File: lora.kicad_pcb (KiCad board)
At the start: 4 copper layers, 80.5 x 45 mm, 64 parts, among them J1 Conn_01x02, J11 Conn_Coaxial, J2 Humidity, J3 Temp, J4 Programming_Jumper, J5 Temp, J6 VDD, J7 GPS, J8 SIM800, J9 I2C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

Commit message: intermediate commit before removing a mounting hole
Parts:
- J1: footprint Connector_PinHeader_2.54mm:PinHeader_1x02_P2.54mm_Vertical -> Connector_PinHeader_2.54mm:PinHeader_1x02_P2.54mm_Horizontal
- J2, J3: footprint Connector_PinHeader_2.54mm:PinHeader_1x03_P2.54mm_Vertical -> Connector_PinHeader_2.54mm:PinHeader_1x03_P2.54mm_Horizontal
- moved J5 76.8 mm to (244.8, 152.2), turned to 180 degrees
- moved R16 61.9 mm to (230.6, 150.8)
- moved R15 60.8 mm to (231.6, 144.6)
- moved J3 53.1 mm to (174.2, 126.8), turned to 180 degrees
- moved J9 51.5 mm to (224.2, 146.2)
- moved R17 50.4 mm to (220.0, 142.0)
- moved J2 49.6 mm to (174.2, 135.6), turned to 180 degrees
- moved Q1 49.4 mm to (177.8, 124.5)
- moved R1 48.4 mm to (177.8, 121.9), turned to 0 degrees
- moved R2 46.6 mm to (181.2, 123.4), turned to 180 degrees
- moved J4 42.3 mm to (214.5, 140.0), turned to 90 degrees
- moved D2 9.24 mm to (177.3, 95.9)
- moved R18 5.48 mm to (172.6, 104.1), turned to 180 degrees
- moved Q4 4.18 mm to (172.1, 101.3), turned to 180 degrees
- moved J1 2.64 mm to (174.2, 97.4), turned to 180 degrees
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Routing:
- net GND: track 139.1 -> 102.6 mm, vias 135 -> 126
- net PRG_JP: track 32.0 -> 0.00 mm
- net I2C_SDA: track 24.4 -> 0.81 mm, vias 1 -> 0
- net I2C_SCL: track 15.4 -> 0.81 mm
- net Net-(J2-Pad1): track 6.39 -> 18.2 mm
- net PRG_TX: track 11.6 -> 0.00 mm
- net PRG_RX: track 9.37 -> 0.00 mm
- net VDD: track 51.2 -> 44.7 mm, vias 18 -> 14
- net RFM_DIO0: track 38.5 -> 44.6 mm
- net ONEWIRE2_DATA: track 32.4 -> 38.2 mm, vias 1 -> 5
- net Net-(D2-Pad1): track 8.63 -> 13.8 mm, vias 0 -> 3
- net ONEWIRE1_DATA: track 38.2 -> 33.4 mm, vias 1 -> 3
- net Net-(J1-Pad2): track 3.69 -> 7.93 mm
- net VDD_SENSOR_MOSFET_SWITCH: track 29.7 -> 33.9 mm, vias 4 -> 2
- net UART2_RX: track 45.0 -> 42.2 mm
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
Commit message: almost done.. more work than expected to change the connector position and size
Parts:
- removed H2: MountingHole_Pad, MountingHole:MountingHole_2.2mm_M2_DIN965_Pad
- moved J5 67.9 mm to (181.1, 128.7)
- moved R17 44.8 mm to (176.4, 132.0), turned to 90 degrees
- moved J4 39.6 mm to (177.4, 126.1), turned to 0 degrees
- moved R16 23.4 mm to (221.3, 129.3)
- moved J9 18.9 mm to (226.5, 127.5)
- moved R15 15.4 mm to (221.2, 133.2), turned to 90 degrees
- moved R2 7.05 mm to (181.4, 116.4), turned to 270 degrees
- moved R1 5.90 mm to (179.8, 116.4), turned to 270 degrees
- moved Q1 5.72 mm to (180.8, 119.7)
- moved R11 2.82 mm to (213.3, 117.7)
- moved R12 2.79 mm to (215.0, 117.7)
- moved Q3 2.78 mm to (214.0, 121.0)
- moved D2 1.14 mm to (176.9, 97.0)
- moved J2 0.38 mm to (173.8, 135.5)
- moved J3 0.38 mm to (173.8, 126.8)
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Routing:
- net I2C_SDA: track 0.81 -> 55.1 mm, vias 0 -> 1
- net I2C_SCL: track 0.81 -> 49.9 mm, vias 0 -> 2
- net PRG_JP: track 0.00 -> 26.0 mm, vias 0 -> 2
- net GPS_MOSFET_SWITCH: track 33.0 -> 14.9 mm, vias 2 -> 0
- net VDD_SENSOR_MOSFET_SWITCH: track 33.9 -> 26.5 mm
- net PRG_TX: track 0.00 -> 5.02 mm
- net Net-(J2-Pad1): track 18.2 -> 23.0 mm
- net PRG_RX: track 0.00 -> 4.03 mm
- net ONEWIRE2_DATA: track 38.2 -> 42.0 mm
- net UART1_TX: track 39.1 -> 42.4 mm
- net UART1_RX: track 32.9 -> 29.8 mm
- net GND: track 102.6 -> 99.6 mm, vias 126 -> 121
- net VDD: track 44.7 -> 47.5 mm, vias 14 -> 16
- net Net-(J7-Pad1): track 2.70 -> 5.49 mm
- net UART2_TX: track 41.7 -> 43.1 mm
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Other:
- outline, holes or cut-outs redrawn
- board text added: "7 - 30V"
- board text added: "W1"
- board text added: "W2"
- board text removed: "7-30V"
- board text removed: "OW1"
- board text removed: "OW2"

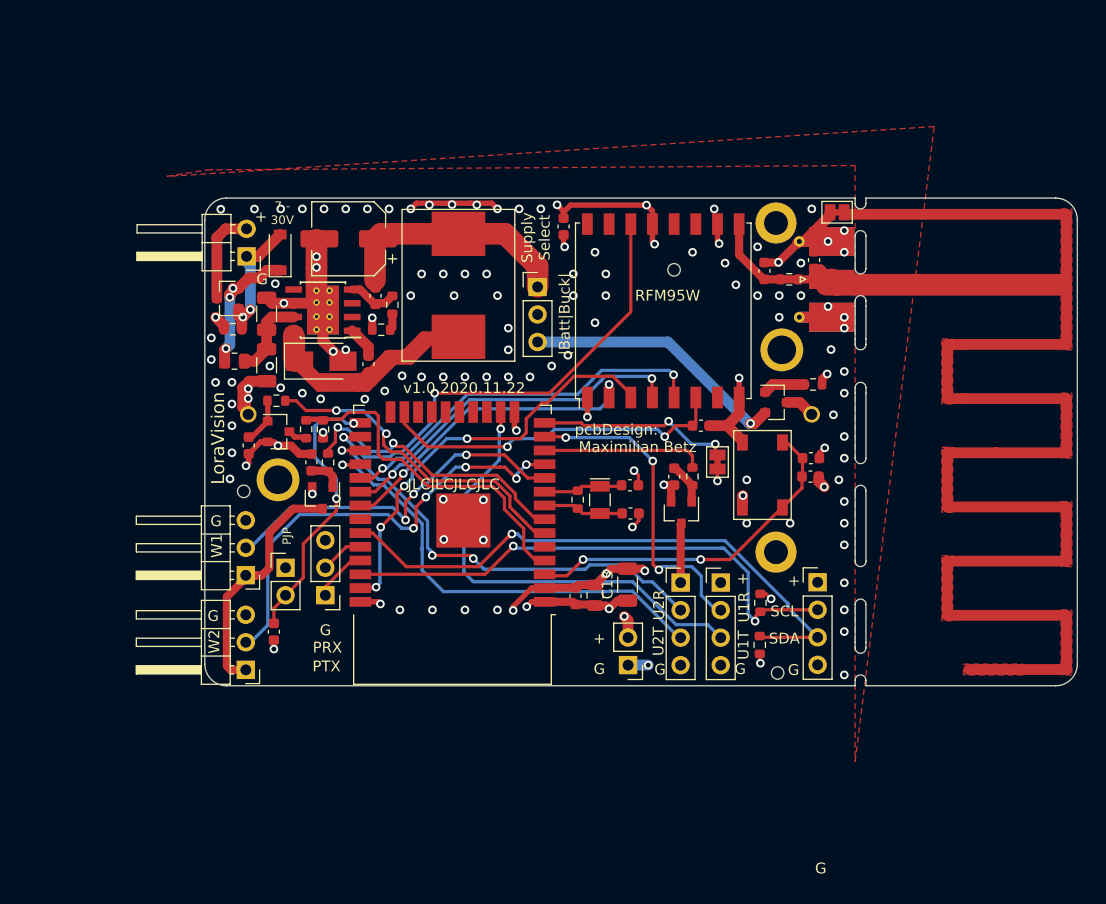
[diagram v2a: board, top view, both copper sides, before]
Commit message: finalized design and exchanges 220u capacity with a one in stock.
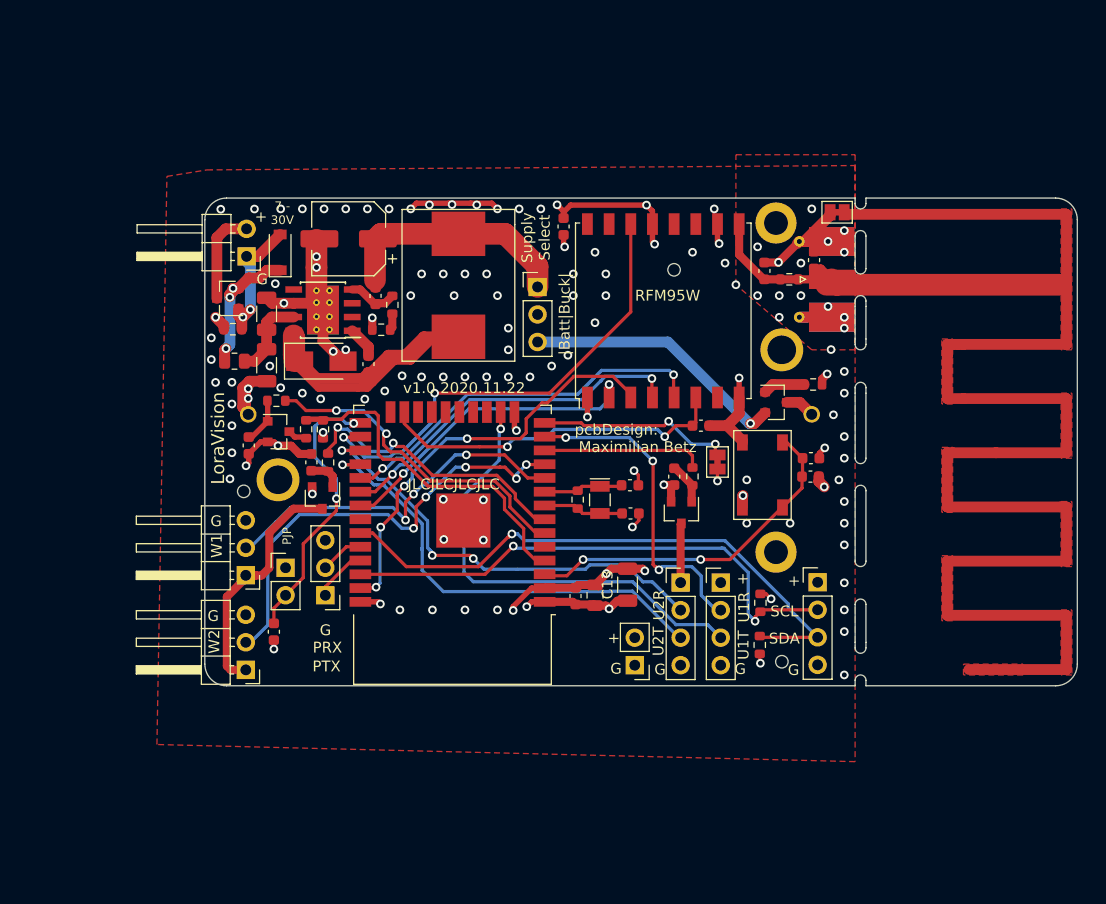
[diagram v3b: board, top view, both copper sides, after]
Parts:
- moved J6 0.62 mm to (209.7, 135.1)
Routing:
- net VDD: track 47.5 -> 45.4 mm, vias 16 -> 15
- net GND: track 99.6 -> 97.8 mm, vias 121 -> 120
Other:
- outline, holes or cut-outs redrawn
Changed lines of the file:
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@@
   (general
     (thickness 1.6)
-    (drawings 80)
-    (tracks 846)
+    (drawings 79)
+    (tracks 841)
     (zones 0)
     (modules 63)
@@
   )
   (module Connector_PinHeader_2.54mm:PinHeader_1x02_P2.54mm_Vertical (layer F.Cu)
-    (at 209.05 135.09 180)
+    (at 209.67 135.1 180)
     (descr "Through hole straight pin header, 1x02, 2.54mm pitch, single row")
     (tags "Through hole pin header THT 1x02 2.54mm single row")
@@
     (effects (font (size 0.8 0.8) (thickness 0.12)))
   )
-  (gr_circle (center 222.85 135.82) (end 223.426 135.82) (layer Edge.Cuts) (width 0.05))
+  (gr_circle (center 223.24 134.78) (end 223.816 134.78) (layer Edge.Cuts) (width 0.05))
   (gr_circle (center 173.59 119.06) (end 174.166 119.06) (layer Edge.Cuts) (width 0.05))
   (gr_circle (center 213.294 98.62) (end 213.87 98.62) (layer Edge.Cuts) (width 0.05))
@@
     (effects (font (size 1 1) (thickness 0.15)))
   )
-  (gr_text G (at 206.4 135.45) (layer F.SilkS)
+  (gr_text G (at 207.94 135.42) (layer F.SilkS)
     (effects (font (size 1 1) (thickness 0.15)))
   )
@@
     (effects (font (size 1 1) (thickness 0.15)))
   )
-  (gr_text + (at 206.4 132.65) (layer F.SilkS)
+  (gr_text + (at 207.74 132.6) (layer F.SilkS)
     (effects (font (size 1 1) (thickness 0.15)))
   )
@@
     (effects (font (size 1 1) (thickness 0.15)))
   )
-  (gr_text G (at 226.83 153.85) (layer F.SilkS)
-    (effects (font (size 1 1) (thickness 0.15)))
-  )
   (gr_text SDA (at 223.47 132.64) (layer F.SilkS)
     (effects (font (size 1 1) (thickness 0.15)))
@@
   (segment (start 180.3 101.74) (end 180.9 102.34) (width 2) (layer F.Cu) (net 2))
   (segment (start 180.3 95.85) (end 180.3 98.4) (width 2) (layer F.Cu) (net 2))
-  (segment (start 209.05 135.09) (end 210.91 135.09) (width 1) (layer B.Cu) (net 2))
   (segment (start 174.005 111.955) (end 174.005 111.805) (width 1) (layer F.Cu) (net 2))
   (segment (start 174.005 111.805) (end 173.5 111.3) (width 1) (layer F.Cu) (net 2))
@@
   (via (at 229 132) (size 0.8) (drill 0.45) (layers F.Cu B.Cu) (net 2))
   (via (at 229 136) (size 0.8) (drill 0.45) (layers F.Cu B.Cu) (net 2))
-  (via (at 210.91 135.09) (size 0.8) (drill 0.45) (layers F.Cu B.Cu) (net 2))
   (via (at 172.32 117.91) (size 0.8) (drill 0.45) (layers F.Cu B.Cu) (net 2))
   (via (at 172.5 115.5) (size 0.8) (drill 0.45) (layers F.Cu B.Cu) (net 2))
@@
   (segment (start 201.35 127.985) (end 200.156998 127.985) (width 0.5) (layer F.Cu) (net 7))
   (segment (start 206.55 127.7) (end 206.35 127.7) (width 0.5) (layer F.Cu) (net 7))
-  (via (at 208.7 130.6) (size 0.8) (drill 0.45) (layers F.Cu B.Cu) (net 7))
-  (segment (start 209.05 130.95) (end 208.7 130.6) (width 1) (layer F.Cu) (net 7))
-  (segment (start 209.05 132.55) (end 209.05 130.95) (width 1) (layer F.Cu) (net 7))
   (via (at 217.3 118.1) (size 0.8) (drill 0.45) (layers F.Cu B.Cu) (net 7))
   (segment (start 217.3 117) (end 217.3 118.1) (width 0.3) (layer F.Cu) (net 7))
@@
     (polygon
       (pts
-        (xy 230 89) (xy 230 144) (xy 237.3 85.4) (xy 166.5 90) (xy 170.2 89.4)
+        (xy 230 89) (xy 230 144) (xy 165.58 142.42) (xy 166.5 90) (xy 170.2 89.4)
       )
     )
@@
     (polygon
       (pts
-        (xy 206.35 130.69) (xy 207.59 131.34) (xy 207.72 144.3) (xy 178.19 143.94) (xy 178.35 130.82)
+        (xy 206.35 130.69) (xy 207.59 131.34) (xy 207.72 144.3) (xy 176.79 143.26) (xy 177.2 130.525)
         (xy 178.93 130.52)
       )
@@
       )
     )
+  )
+  (zone (net 2) (net_name GND) (layer F.Cu) (hatch edge 0.508)
+    (connect_pads yes (clearance 0))
+    (min_thickness 0.254)
+    (fill yes (arc_segments 32) (thermal_gap 0.508) (thermal_bridge_width 0.508))
+    (polygon
+      (pts
+        (xy 230 106) (xy 226 106) (xy 219 100) (xy 219 88) (xy 230 88)
+      )
+    )

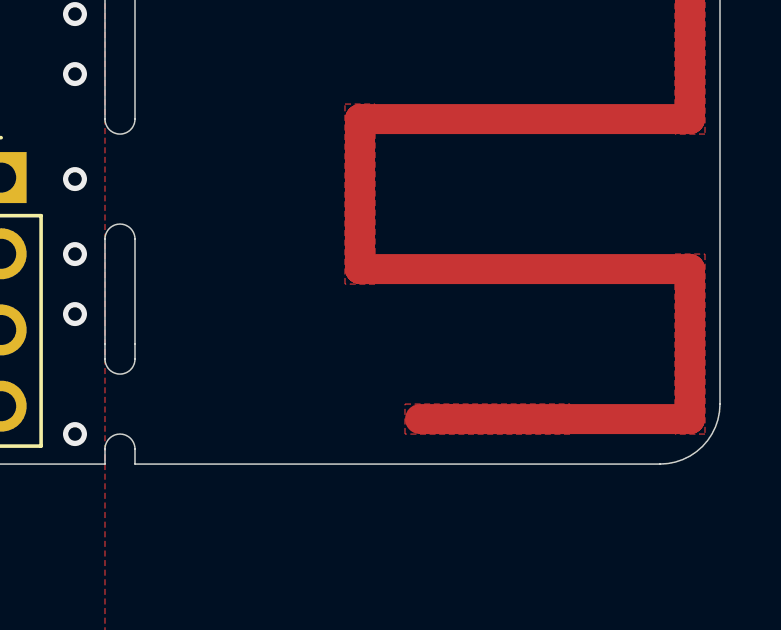
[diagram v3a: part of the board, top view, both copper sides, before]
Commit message: added cut line for antenna cut in PVC tube enclosure.
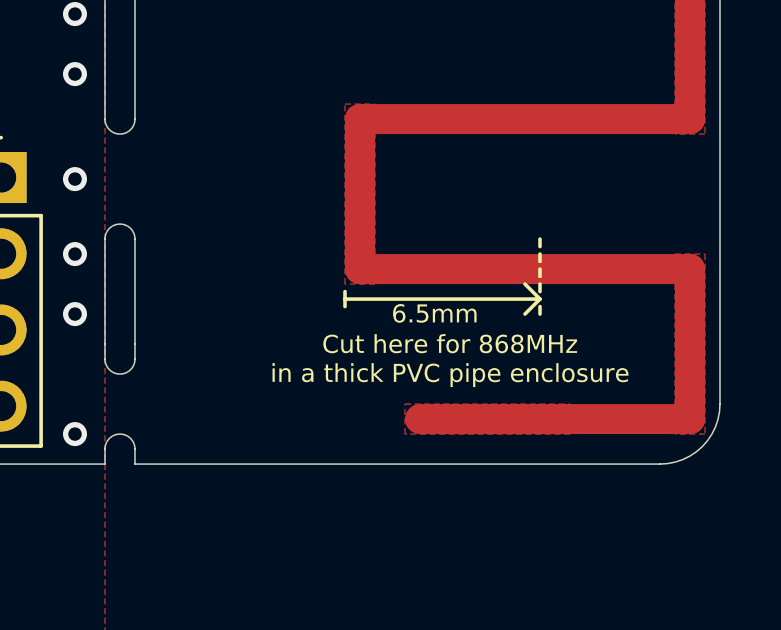
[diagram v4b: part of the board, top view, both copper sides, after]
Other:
- board text added: "6.5mm"
- board text added: "Cut here for 868MHz in a thick PVC pipe enclosure"

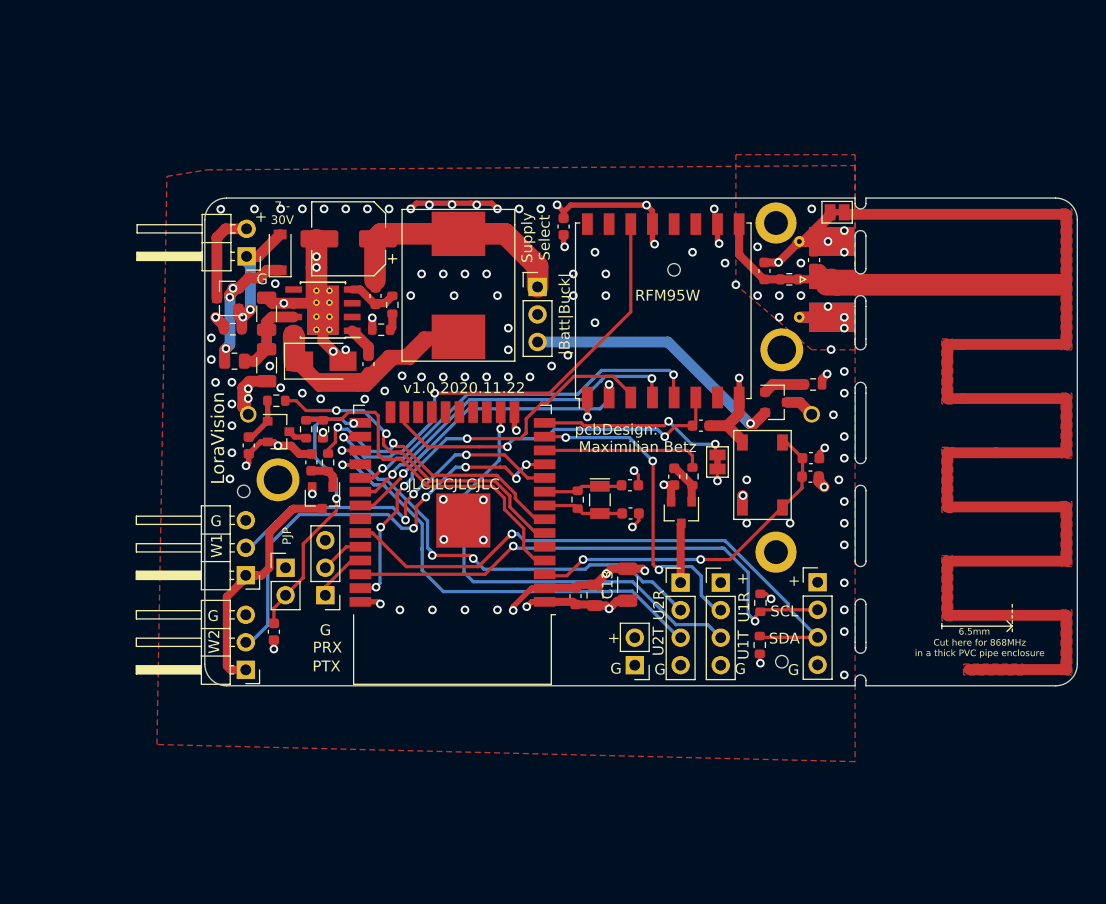
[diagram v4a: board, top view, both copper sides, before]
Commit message: remove JP2, add hints for StepUP DCDC
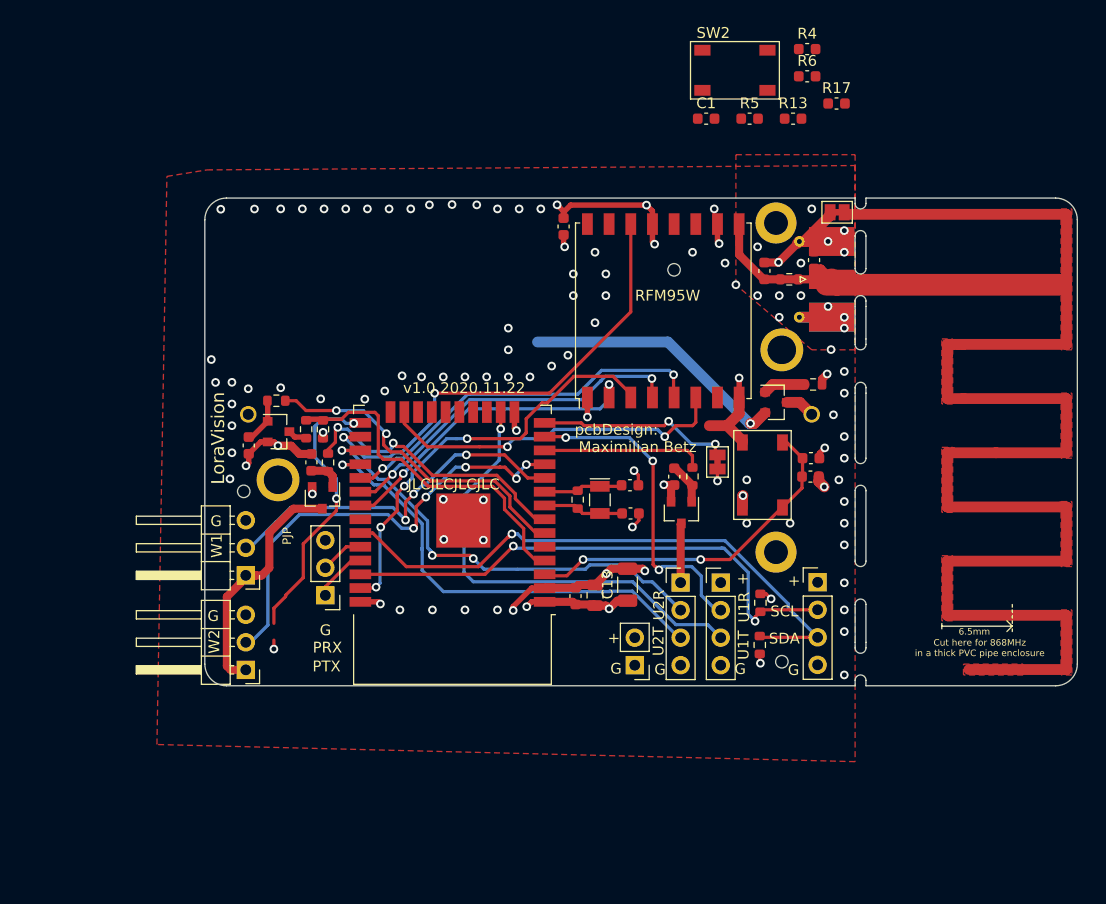
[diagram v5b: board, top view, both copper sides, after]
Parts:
- removed C2: 10u, Capacitor_SMD:C_1206_3216Metric
- removed C3: 100n, Capacitor_SMD:C_0603_1608Metric
- removed C4: 220u, Capacitor_SMD:CP_Elec_6.3x7.7
- removed D1: SS34, Diode_SMD:D_SMA
- removed D2: MM1Z15, Diode_SMD:D_SOD-123
- removed FB1: Ferrite_Bead_Small, Resistor_SMD:R_0805_2012Metric
- removed J1: Conn_01x02, Connector_PinHeader_2.54mm:PinHeader_1x02_P2.54mm_Horizontal
- removed J4: Programming_Jumper, Connector_PinHeader_2.54mm:PinHeader_1x02_P2.54mm_Vertical
- removed L1: 22u, OWN_Parts_:L_MS1040-220M
- removed Q4: AO3401A, Package_TO_SOT_SMD:SOT-23
- removed R18: 100k, Resistor_SMD:R_0603_1608Metric
- removed U1: TPS5430DDA, Package_SO:TI_SO-PowerPAD-8_ThermalVias
- C1: value 10u -> 100n; footprint Capacitor_SMD:C_1206_3216Metric -> Capacitor_SMD:C_0603_1608Metric
- R5: value 5.1k -> 10k; footprint Resistor_SMD:R_0603_1608Metric -> Capacitor_SMD:C_0603_1608Metric
- R6: value 240 -> 10k; footprint Resistor_SMD:R_0603_1608Metric -> Capacitor_SMD:C_0603_1608Metric
- SW2: value VDD_Selector -> PJ; footprint Connector_PinHeader_2.54mm:PinHeader_1x03_P2.54mm_Vertical -> OWN_Parts_:TS-1187A-C-E-B
- moved R17 71.2 mm to (228.3, 83.3), turned to 0 degrees
- moved R4 45.9 mm to (225.6, 78.3), turned to 0 degrees
- moved R6 45.7 mm to (225.6, 80.8), turned to 0 degrees
- moved C1 44.4 mm to (216.3, 84.7), turned to 0 degrees
- moved R5 37.2 mm to (220.3, 84.7), turned to 0 degrees
- moved R13 29.6 mm to (224.3, 84.7)
- moved SW2 26.9 mm to (218.9, 80.4)
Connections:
- C1 pad 2: VSUPPLY -> PRG_JP
- C13 pad 2: VDD -> VBATT
- C6 pad 2: VDD -> VBATT
- C7 pad 2: VDD -> VBATT
- C9 pad 2: VDD -> VBATT
- J6 pad 2: VDD -> VBATT
- J8 pad 1: VDD -> VBATT
- J9 pad 1: VDD -> VBATT
- JP2 pad 2: VDD -> VBATT
- Q1 pad 2: VDD -> VBATT
- Q2 pad 2: VDD -> VBATT
- Q3 pad 2: VDD -> VBATT
- R1 pad 1: VDD -> VBATT
- R11 pad 1: VDD -> VBATT
- R13 pad 1: RFM_RST -> VBATT
- R13 pad 2: GND -> SPI_MISO
- R15 pad 1: VDD -> VBATT
- R16 pad 1: VDD -> VBATT
- R17 pad 1: VDD -> VBATT
- R17 pad 2: PRG_JP -> SPI_CS
- R3 pad 2: VDD -> VBATT
- R4 pad 1: Net-(C4-Pad1) -> PRG_JP
- R4 pad 2: Net-(R4-Pad2) -> VBATT
- R5 pad 1: Net-(R4-Pad2) -> VBATT
- R5 pad 2: Net-(R5-Pad2) -> SPI_SCK
- R6 pad 1: Net-(R5-Pad2) -> VBATT
- R6 pad 2: GND -> SPI_MOSI
- R9 pad 1: VDD -> VBATT
- SW2 pad 1: Net-(C4-Pad1) -> GND
- SW2 pad 2: VDD -> GND
- SW2 pad 3: VBATT -> PRG_JP
- U2 pad 2: VDD -> VBATT
- U4 pad 13: VDD -> VBATT
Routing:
- net VDD: track 45.4 -> 0.00 mm, vias 15 -> 0
- net VBATT: track 24.5 -> 70.0 mm, vias 1 -> 16
- net Net-(C3-Pad1): track 45.0 -> 0.00 mm
- net GND: track 97.8 -> 54.9 mm, vias 120 -> 101
- net Net-(C4-Pad1): track 26.7 -> 0.00 mm
- net Net-(D2-Pad2): track 14.1 -> 0.00 mm, vias 2 -> 0
- net Net-(D2-Pad1): track 13.0 -> 0.00 mm, vias 3 -> 0
- net Net-(J1-Pad2): track 9.11 -> 0.00 mm
- net VSUPPLY: track 7.70 -> 0.00 mm
- net Net-(R4-Pad2): track 4.59 -> 0.00 mm
- net Net-(C3-Pad2): track 2.93 -> 0.00 mm
- net Net-(R5-Pad2): track 1.56 -> 0.00 mm
- added copper zone on In2.Cu_VDD, net VBATT
- removed copper zone on In2.Cu_VDD, net VDD
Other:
- board text added: "-"
- board text added: "LifePo4 or Lithium-Thionyl-Chlorid 3.6V MAX!"
- board text removed: "7 - 30V"
- board text removed: "Supply Select"
- board text removed: "|Batt|Buck|"
